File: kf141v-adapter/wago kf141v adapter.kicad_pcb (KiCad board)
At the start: 2 copper layers, 15.5 x 30 mm, 2 parts, among them J1 Conn_01x10, J2 Conn_01x10

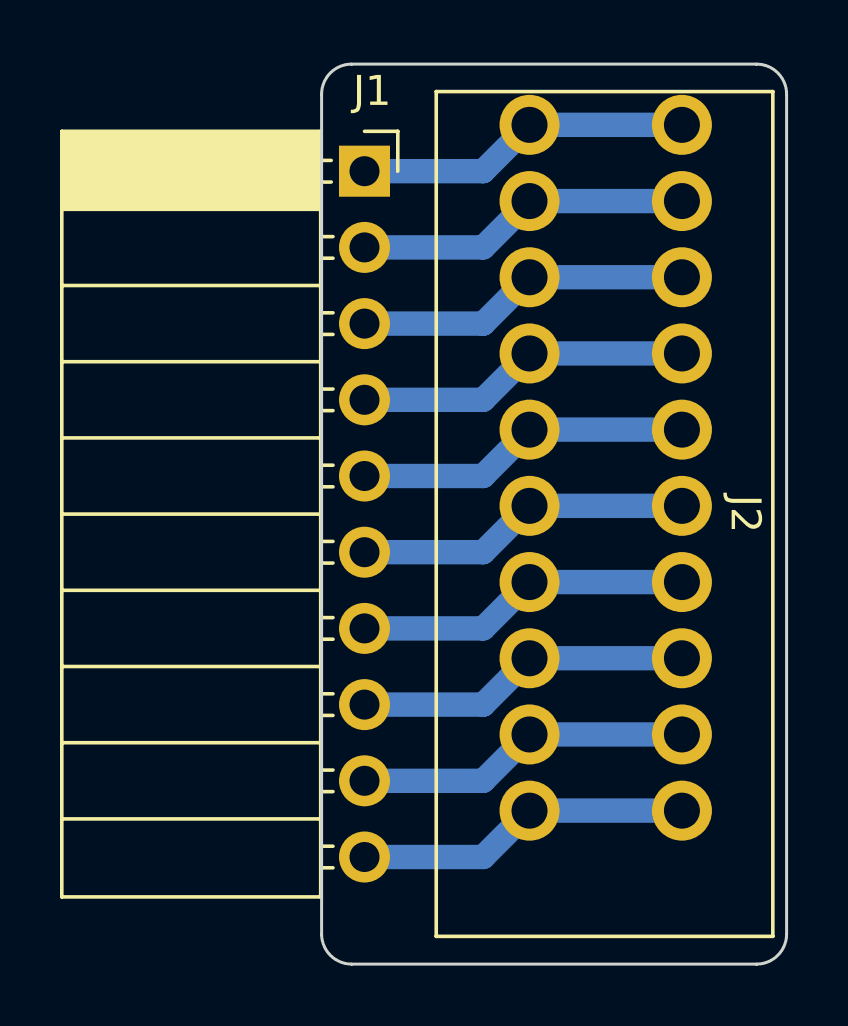
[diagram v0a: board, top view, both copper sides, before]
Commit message: KF141 adapters REV2 - tighter spacing.
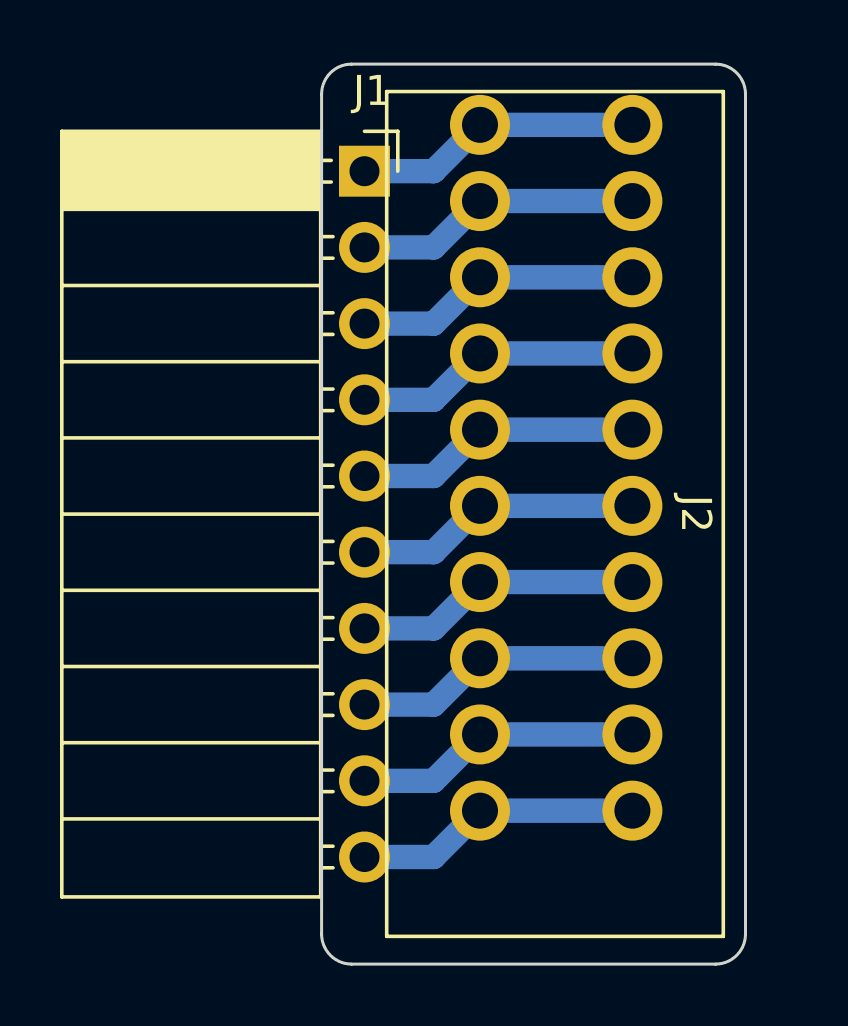
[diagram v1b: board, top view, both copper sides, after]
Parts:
- moved J2 1.65 mm to (144.8, 87.0)
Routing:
- net Net-(J1-Pin_9): track 11.2 -> 9.57 mm
- net Net-(J1-Pin_8): track 11.2 -> 9.57 mm
- net Net-(J1-Pin_7): track 11.2 -> 9.57 mm
- net Net-(J1-Pin_6): track 11.2 -> 9.57 mm
- net Net-(J1-Pin_5): track 11.2 -> 9.57 mm
- net Net-(J1-Pin_4): track 11.2 -> 9.57 mm
- net Net-(J1-Pin_3): track 11.2 -> 9.57 mm
- net Net-(J1-Pin_2): track 11.2 -> 9.57 mm
- net Net-(J1-Pin_10): track 11.2 -> 9.57 mm
- net Net-(J1-Pin_1): track 11.2 -> 9.57 mm
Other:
- board size 15.5 x 30 mm -> 14.1 x 30 mm
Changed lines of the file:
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@@
       (plotinvisibletext false)
       (sketchpadsonfab false)
-      (subtractmaskfromsilk false)
+      (subtractmaskfromsilk true)
       (outputformat 1)
       (mirror false)
@@
   )
   (footprint "dp_connector:wago_kf141v_2.54" (layer "F.Cu")
-    (at 146.431 86.995 -90)
+    (at 144.78 86.995 -90)
     (property "Sheetfile" "wago kf141v adapter.kicad_sch")
     (property "Sheetname" "")
@@
       (net 10 "Net-(J1-Pin_10)") (pinfunction "Pin_10") (pintype "passive"))
   )
-  (gr_line (start 138 72) (end 151.5 72)
-    (stroke (width 0.1) (type default)) (layer "Edge.Cuts"))
-  (gr_line (start 138 102) (end 151.5 102)
+  (gr_line (start 138 72) (end 150.13 72)
+    (stroke (width 0.1) (type default)) (layer "Edge.Cuts"))
+  (gr_line (start 138 102) (end 150.13 102)
     (stroke (width 0.1) (type default)) (layer "Edge.Cuts"))
   (gr_line (start 137 73) (end 137 101)
     (stroke (width 0.1) (type default)) (layer "Edge.Cuts"))
-  (gr_arc (start 152.5 101) (mid 152.207107 101.707107) (end 151.5 102)
-    (stroke (width 0.1) (type default)) (layer "Edge.Cuts"))
-  (gr_arc (start 151.5 72) (mid 152.207107 72.292893) (end 152.5 73)
-    (stroke (width 0.1) (type default)) (layer "Edge.Cuts"))
-  (gr_line (start 152.5 73) (end 152.5 101)
+  (gr_arc (start 151.13 101) (mid 150.837107 101.707107) (end 150.13 102)
+    (stroke (width 0.1) (type default)) (layer "Edge.Cuts"))
+  (gr_arc (start 150.13 72) (mid 150.837107 72.292893) (end 151.13 73)
+    (stroke (width 0.1) (type default)) (layer "Edge.Cuts"))
+  (gr_line (start 151.13 73) (end 151.13 101)
     (stroke (width 0.1) (type default)) (layer "Edge.Cuts"))
   (gr_arc (start 138 102) (mid 137.292893 101.707107) (end 137 101)
@@
   (gr_arc (start 137 73) (mid 137.292893 72.292893) (end 138 72)
     (stroke (width 0.1) (type default)) (layer "Edge.Cuts"))
-  (segment (start 138.43 75.57) (end 142.386 75.57) (width 0.8128) (layer "B.Cu") (net 1))
-  (segment (start 142.386 75.57) (end 143.931 74.025) (width 0.8128) (layer "B.Cu") (net 1))
-  (segment (start 143.931 74.025) (end 149.011 74.025) (width 0.8128) (layer "B.Cu") (net 1))
-  (segment (start 138.43 78.11) (end 142.386 78.11) (width 0.8128) (layer "B.Cu") (net 2))
-  (segment (start 143.931 76.565) (end 149.011 76.565) (width 0.8128) (layer "B.Cu") (net 2))
-  (segment (start 142.386 78.11) (end 143.931 76.565) (width 0.8128) (layer "B.Cu") (net 2))
-  (segment (start 149.011 79.105) (end 143.931 79.105) (width 0.8128) (layer "B.Cu") (net 3))
-  (segment (start 142.386 80.65) (end 143.931 79.105) (width 0.8128) (layer "B.Cu") (net 3))
-  (segment (start 138.43 80.65) (end 142.386 80.65) (width 0.8128) (layer "B.Cu") (net 3))
-  (segment (start 138.43 83.19) (end 142.386 83.19) (width 0.8128) (layer "B.Cu") (net 4))
-  (segment (start 143.931 81.645) (end 149.011 81.645) (width 0.8128) (layer "B.Cu") (net 4))
-  (segment (start 142.386 83.19) (end 143.931 81.645) (width 0.8128) (layer "B.Cu") (net 4))
-  (segment (start 142.386 85.73) (end 143.931 84.185) (width 0.8128) (layer "B.Cu") (net 5))
-  (segment (start 149.011 84.185) (end 143.931 84.185) (width 0.8128) (layer "B.Cu") (net 5))
-  (segment (start 138.43 85.73) (end 142.386 85.73) (width 0.8128) (layer "B.Cu") (net 5))
-  (segment (start 143.931 86.725) (end 149.011 86.725) (width 0.8128) (layer "B.Cu") (net 6))
-  (segment (start 142.386 88.27) (end 143.931 86.725) (width 0.8128) (layer "B.Cu") (net 6))
-  (segment (start 138.43 88.27) (end 142.386 88.27) (width 0.8128) (layer "B.Cu") (net 6))
-  (segment (start 142.386 90.81) (end 143.931 89.265) (width 0.8128) (layer "B.Cu") (net 7))
-  (segment (start 138.43 90.81) (end 142.386 90.81) (width 0.8128) (layer "B.Cu") (net 7))
-  (segment (start 149.011 89.265) (end 143.931 89.265) (width 0.8128) (layer "B.Cu") (net 7))
-  (segment (start 142.386 93.35) (end 143.931 91.805) (width 0.8128) (layer "B.Cu") (net 8))
-  (segment (start 138.43 93.35) (end 142.386 93.35) (width 0.8128) (layer "B.Cu") (net 8))
-  (segment (start 143.931 91.805) (end 149.011 91.805) (width 0.8128) (layer "B.Cu") (net 8))
-  (segment (start 142.386 95.89) (end 143.931 94.345) (width 0.8128) (layer "B.Cu") (net 9))
-  (segment (start 138.43 95.89) (end 142.386 95.89) (width 0.8128) (layer "B.Cu") (net 9))
-  (segment (start 149.011 94.345) (end 143.931 94.345) (width 0.8128) (layer "B.Cu") (net 9))
-  (segment (start 138.43 98.43) (end 142.386 98.43) (width 0.8128) (layer "B.Cu") (net 10))
-  (segment (start 142.386 98.43) (end 143.931 96.885) (width 0.8128) (layer "B.Cu") (net 10))
-  (segment (start 143.931 96.885) (end 149.011 96.885) (width 0.8128) (layer "B.Cu") (net 10))
+  (segment (start 142.28 74.025) (end 147.36 74.025) (width 0.8128) (layer "B.Cu") (net 1))
+  (segment (start 140.735 75.57) (end 142.28 74.025) (width 0.8128) (layer "B.Cu") (net 1))
+  (segment (start 138.43 75.57) (end 140.735 75.57) (width 0.8128) (layer "B.Cu") (net 1))
+  (segment (start 142.28 76.565) (end 147.36 76.565) (width 0.8128) (layer "B.Cu") (net 2))
+  (segment (start 140.735 78.11) (end 142.28 76.565) (width 0.8128) (layer "B.Cu") (net 2))
+  (segment (start 138.43 78.11) (end 140.735 78.11) (width 0.8128) (layer "B.Cu") (net 2))
+  (segment (start 140.735 80.65) (end 142.28 79.105) (width 0.8128) (layer "B.Cu") (net 3))
+  (segment (start 147.36 79.105) (end 142.28 79.105) (width 0.8128) (layer "B.Cu") (net 3))
+  (segment (start 138.43 80.65) (end 140.735 80.65) (width 0.8128) (layer "B.Cu") (net 3))
+  (segment (start 138.43 83.19) (end 140.735 83.19) (width 0.8128) (layer "B.Cu") (net 4))
+  (segment (start 140.735 83.19) (end 142.28 81.645) (width 0.8128) (layer "B.Cu") (net 4))
+  (segment (start 142.28 81.645) (end 147.36 81.645) (width 0.8128) (layer "B.Cu") (net 4))
+  (segment (start 140.735 85.73) (end 142.28 84.185) (width 0.8128) (layer "B.Cu") (net 5))
+  (segment (start 147.36 84.185) (end 142.28 84.185) (width 0.8128) (layer "B.Cu") (net 5))
+  (segment (start 138.43 85.73) (end 140.735 85.73) (width 0.8128) (layer "B.Cu") (net 5))
+  (segment (start 138.43 88.27) (end 140.735 88.27) (width 0.8128) (layer "B.Cu") (net 6))
+  (segment (start 142.28 86.725) (end 147.36 86.725) (width 0.8128) (layer "B.Cu") (net 6))
+  (segment (start 140.735 88.27) (end 142.28 86.725) (width 0.8128) (layer "B.Cu") (net 6))
+  (segment (start 147.36 89.265) (end 142.28 89.265) (width 0.8128) (layer "B.Cu") (net 7))
+  (segment (start 140.735 90.81) (end 142.28 89.265) (width 0.8128) (layer "B.Cu") (net 7))
+  (segment (start 138.43 90.81) (end 140.735 90.81) (width 0.8128) (layer "B.Cu") (net 7))
+  (segment (start 138.43 93.35) (end 140.735 93.35) (width 0.8128) (layer "B.Cu") (net 8))
+  (segment (start 142.28 91.805) (end 147.36 91.805) (width 0.8128) (layer "B.Cu") (net 8))
+  (segment (start 140.735 93.35) (end 142.28 91.805) (width 0.8128) (layer "B.Cu") (net 8))
+  (segment (start 147.36 94.345) (end 142.28 94.345) (width 0.8128) (layer "B.Cu") (net 9))
+  (segment (start 140.735 95.89) (end 142.28 94.345) (width 0.8128) (layer "B.Cu") (net 9))
+  (segment (start 138.43 95.89) (end 140.735 95.89) (width 0.8128) (layer "B.Cu") (net 9))
+  (segment (start 138.43 98.43) (end 140.735 98.43) (width 0.8128) (layer "B.Cu") (net 10))
+  (segment (start 140.735 98.43) (end 142.28 96.885) (width 0.8128) (layer "B.Cu") (net 10))
+  (segment (start 142.28 96.885) (end 147.36 96.885) (width 0.8128) (layer "B.Cu") (net 10))
 )
